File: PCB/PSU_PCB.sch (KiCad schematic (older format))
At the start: 116 parts, among them P1 Bluetooth HM-10, P2 ISP, P3 V+, P4 V-, Q1 IRLML0030TRPBF, Q2 IRLML0030TRPBF, SW1 SW_PUSH_SMALL_H, U1 OPA2170, U10 LT3080, U11 LM334M, U2 USB_TYPE_C, U3 ATMEGA32U4RC-A, U4 MCP41010, U5 LT1370, U6 MAX6610, U7 OPA4170, U8 INA219, U9 MCP1252, Y1 16Mhz

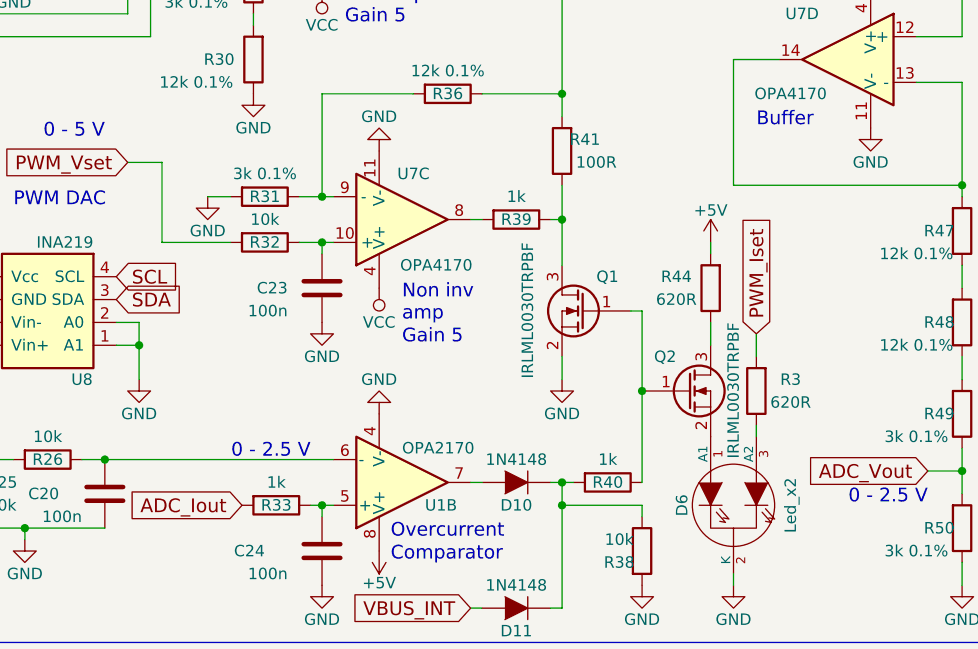
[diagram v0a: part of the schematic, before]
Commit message: Fixed minor PCB error Adjusted code for current measurement
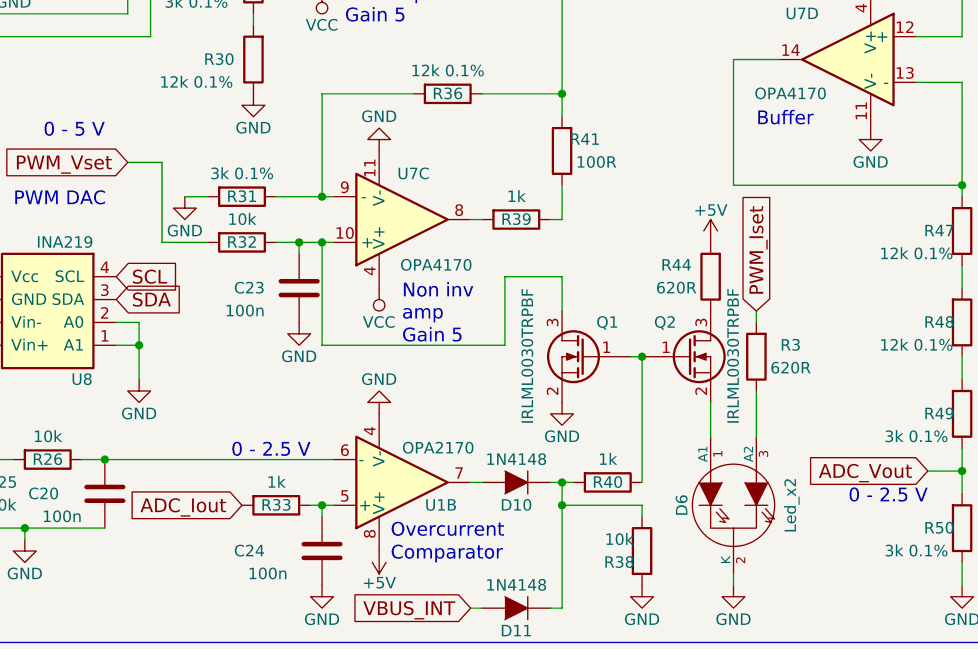
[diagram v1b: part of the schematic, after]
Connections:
- net at C23.2, R32.1, U7.10 (+): now also Q1.3 (D)
- net at R39.1, R41.1: no longer Q1.3 (D)
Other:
- moved on the sheet: C23, Q1, Q2, R3, R31, R32, R44
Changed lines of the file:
@@
 L R R31
 U 1 1 57B3FFF3
-P 7800 3200
-F 0 "R31" V 7800 3200 50  0000 C CNN
-F 1 "3k 0.1%" V 7700 3200 50  0000 C CNN
-F 2 "Resistors_SMD:R_0603_HandSoldering" V 7730 3200 50  0001 C CNN
-F 3 "" H 7800 3200 50  0000 C CNN
-	1    7800 3200
+P 7700 3200
+F 0 "R31" V 7700 3200 50  0000 C CNN
+F 1 "3k 0.1%" V 7600 3200 50  0000 C CNN
+F 2 "Resistors_SMD:R_0603_HandSoldering" V 7630 3200 50  0001 C CNN
+F 3 "" H 7700 3200 50  0000 C CNN
+	1    7700 3200
 	0    1    1    0
 $EndComp
@@
 L GND #PWR015
 U 1 1 57B40093
-P 7550 3200
-F 0 "#PWR015" H 7550 2950 50  0001 C CNN
-F 1 "GND" H 7550 3050 50  0000 C CNN
-F 2 "" H 7550 3200 50  0000 C CNN
-F 3 "" H 7550 3200 50  0000 C CNN
-	1    7550 3200
+P 7450 3200
+F 0 "#PWR015" H 7450 2950 50  0001 C CNN
+F 1 "GND" H 7450 3050 50  0000 C CNN
+F 2 "" H 7450 3200 50  0000 C CNN
+F 3 "" H 7450 3200 50  0000 C CNN
+	1    7450 3200
 	1    0    0    -1
 $EndComp
@@
 L R R32
 U 1 1 57B47B3D
-P 7800 3400
-F 0 "R32" V 7800 3400 50  0000 C CNN
-F 1 "10k" V 7700 3400 50  0000 C CNN
-F 2 "Resistors_SMD:R_0603_HandSoldering" V 7730 3400 50  0001 C CNN
-F 3 "" H 7800 3400 50  0000 C CNN
-	1    7800 3400
+P 7700 3400
+F 0 "R32" V 7700 3400 50  0000 C CNN
+F 1 "10k" V 7600 3400 50  0000 C CNN
+F 2 "Resistors_SMD:R_0603_HandSoldering" V 7630 3400 50  0001 C CNN
+F 3 "" H 7700 3400 50  0000 C CNN
+	1    7700 3400
 	0    1    1    0
 $EndComp
@@
 L C C23
 U 1 1 57B48497
-P 8050 3600
-F 0 "C23" H 8200 3600 50  0000 L CNN
-F 1 "100n" H 8200 3700 50  0000 L CNN
-F 2 "Capacitors_SMD:C_0603_HandSoldering" H 8088 3450 50  0001 C CNN
-F 3 "" H 8050 3600 50  0000 C CNN
-	1    8050 3600
+P 7950 3600
+F 0 "C23" H 8100 3600 50  0000 L CNN
+F 1 "100n" H 8100 3700 50  0000 L CNN
+F 2 "Capacitors_SMD:C_0603_HandSoldering" H 7988 3450 50  0001 C CNN
+F 3 "" H 7950 3600 50  0000 C CNN
+	1    7950 3600
 	-1   0    0    1
 $EndComp
@@
 L GND #PWR016
 U 1 1 57B48873
-P 8050 3750
-F 0 "#PWR016" H 8050 3500 50  0001 C CNN
-F 1 "GND" H 8050 3600 50  0000 C CNN
-F 2 "" H 8050 3750 50  0000 C CNN
-F 3 "" H 8050 3750 50  0000 C CNN
-	1    8050 3750
+P 7950 3750
+F 0 "#PWR016" H 7950 3500 50  0001 C CNN
+F 1 "GND" H 7950 3600 50  0000 C CNN
+F 2 "" H 7950 3750 50  0000 C CNN
+F 3 "" H 7950 3750 50  0000 C CNN
+	1    7950 3750
 	1    0    0    -1
 $EndComp
@@
 L R R44
 U 1 1 57B99CDC
-P 9750 3600
-F 0 "R44" H 9900 3550 50  0000 C CNN
-F 1 "620R" H 9900 3650 50  0000 C CNN
-F 2 "Resistors_SMD:R_0603_HandSoldering" V 9680 3600 50  0001 C CNN
-F 3 "" H 9750 3600 50  0000 C CNN
-	1    9750 3600
+P 9750 3550
+F 0 "R44" H 9900 3500 50  0000 C CNN
+F 1 "620R" H 9900 3600 50  0000 C CNN
+F 2 "Resistors_SMD:R_0603_HandSoldering" V 9680 3550 50  0001 C CNN
+F 3 "" H 9750 3550 50  0000 C CNN
+	1    9750 3550
 	-1   0    0    1
 $EndComp
@@
 8E D2 4E 06 E9 83 31 0C B8 01 D4 62 7A FA FE CA 1E E7 AB A8 50 4D B8 D1 52 86 A6 EF 44 4C F7 6B
 69 A6 CB 4C 71 E1 73 B8 2B 4F 00 E7 75 28 F9 2E A2 C6 63 AC 40 DB 07 B2 19 61 39 9A 3C 4A F1 B4
-F5 AD 2E B3 0D FC 7F 6D 80 3F 3C 28 70 B1 D5 00 00 00 00 49 45 4E 44 AE 42 60 82 D1
+F5 AD 2E B3 0D FC 7F 6D 80 3F 3C 28 70 B1 D5 00 00 00 00 49 45 4E 44 AE 42 60 82 66
 EndData
 $EndBitmap
@@
 00 09 E8 04 41 10 04 61 00 48 40 27 08 82 20 08 03 40 02 3A 41 10 04 41 18 00 23 00 F5 5D DD 09
 82 20 08 82 20 B4 52 CF 06 60 0D 60 1C 9A D7 A4 13 04 41 10 04 D1 BD 50 00 7E F8 7F 36 C9 A5 48
-A4 FE A8 58 00 00 00 00 49 45 4E 44 AE 42 60 82 20
+A4 FE A8 58 00 00 00 00 49 45 4E 44 AE 42 60 82 40
 EndData
 $EndBitmap
@@
 L GND #PWR038
 U 1 1 58E93020
-P 9100 4000
-F 0 "#PWR038" H 9100 3750 50  0001 C CNN
-F 1 "GND" H 9100 3850 50  0000 C CNN
-F 2 "" H 9100 4000 50  0000 C CNN
-F 3 "" H 9100 4000 50  0000 C CNN
-	1    9100 4000
+P 9100 4100
+F 0 "#PWR038" H 9100 3850 50  0001 C CNN
+F 1 "GND" H 9100 3950 50  0000 C CNN
+F 2 "" H 9100 4100 50  0000 C CNN
+F 3 "" H 9100 4100 50  0000 C CNN
+	1    9100 4100
 	1    0    0    -1
 $EndComp
@@
 L Q_NMOS_GSD Q1
 U 1 1 59B69DD1
-P 9200 3700
-F 0 "Q1" H 9150 3850 50  0000 R CNN
-F 1 "IRLML0030TRPBF" V 9450 4000 50  0000 R CNN
-F 2 "TO_SOT_Packages_SMD:SOT-23" H 9400 3800 50  0001 C CNN
-F 3 "" H 9200 3700 50  0000 C CNN
-	1    9200 3700
+P 9200 3900
+F 0 "Q1" H 9150 4050 50  0000 R CNN
+F 1 "IRLML0030TRPBF" V 9450 4200 50  0000 R CNN
+F 2 "TO_SOT_Packages_SMD:SOT-23" H 9400 4000 50  0001 C CNN
+F 3 "" H 9200 3900 50  0000 C CNN
+	1    9200 3900
 	-1   0    0    -1
 $EndComp
@@
 L Q_NMOS_GSD Q2
 U 1 1 59C405FE
-P 9650 4050
-F 0 "Q2" H 9600 4200 50  0000 R CNN
-F 1 "IRLML0030TRPBF" V 9850 4350 50  0000 R CNN
-F 2 "TO_SOT_Packages_SMD:SOT-23" H 9850 4150 50  0001 C CNN
-F 3 "" H 9650 4050 50  0000 C CNN
-	1    9650 4050
+P 9650 3900
+F 0 "Q2" H 9600 4050 50  0000 R CNN
+F 1 "IRLML0030TRPBF" V 9850 4200 50  0000 R CNN
+F 2 "TO_SOT_Packages_SMD:SOT-23" H 9850 4000 50  0001 C CNN
+F 3 "" H 9650 3900 50  0000 C CNN
+	1    9650 3900
 	1    0    0    -1
 $EndComp
@@
 	0    -1   -1   0
 $EndComp
-Text GLabel 9950 3800 1    60   Input ~ 0
+Text GLabel 9950 3700 1    60   Input ~ 0
 PWM_Iset
 $Comp
 L R R3
 U 1 1 59D48892
-P 9950 4050
-F 0 "R3" H 9800 4000 50  0000 C CNN
-F 1 "620R" H 9800 4100 50  0000 C CNN
-F 2 "Resistors_SMD:R_0603_HandSoldering" V 9880 4050 50  0001 C CNN
-F 3 "" H 9950 4050 50  0000 C CNN
-	1    9950 4050
+P 9950 3900
+F 0 "R3" H 9800 3850 50  0000 C CNN
+F 1 "620R" H 9800 3950 50  0000 C CNN
+F 2 "Resistors_SMD:R_0603_HandSoldering" V 9880 3900 50  0001 C CNN
+F 3 "" H 9950 3900 50  0000 C CNN
+	1    9950 3900
 	-1   0    0    1
 $EndComp
@@
 Wire Wire Line
 	9850 4900 9850 4850
-Connection ~ 9450 4050
+Connection ~ 9450 3900
 Wire Wire Line
 	8750 4450 8700 4450
@@
 	5350 3650 4100 3650
 Wire Wire Line
-	9950 3900 9950 3800
+	9950 3750 9950 3700
 Wire Wire Line
-	9950 4250 9950 4200
+	9950 4250 9950 4050
 Wire Wire Line
 	4300 2650 4300 2150
@@
 	9850 3150 9850 2600
 Wire Wire Line
-	7350 3400 7650 3400
+	7350 3400 7550 3400
 Wire Wire Line
 	6500 3650 6500 4000
@@
 Connection ~ 10600 1050
 Wire Wire Line
-	9750 3750 9750 3850
+	9750 3700 9750 3700
 Connection ~ 6200 1050
 Wire Wire Line
@@
 Connection ~ 10000 1050
 Wire Wire Line
-	7550 3200 7650 3200
+	7450 3200 7550 3200
 Wire Wire Line
-	7950 3200 8100 3200
-Wire Wire Line
-	9100 3150 9100 3500
+	7850 3200 8100 3200
 Connection ~ 8050 3200
 Wire Wire Line
@@
 Connection ~ 9100 2750
 Wire Wire Line
-	7950 3400 8100 3400
+	7850 3400 8100 3400
 Wire Wire Line
-	8050 3450 8050 3400
-Connection ~ 8050 3400
-Connection ~ 9100 3300
+	7950 3450 7950 3400
+Connection ~ 7950 3400
 Wire Wire Line
 	8000 4550 8100 4550
@@
 	6350 3550 6550 3550
 Wire Wire Line
-	9750 3400 9750 3450
+	9750 3400 9750 3400
 Wire Wire Line
 	4200 3000 4950 3000
@@
 Connection ~ 10150 1850
 Wire Wire Line
-	9100 3900 9100 4000
-Wire Wire Line
 	4200 2900 5150 2900
 Wire Wire Line
@@
 	6950 7750 6950 6750
 Wire Wire Line
-	9450 3700 9400 3700
+	9450 3900 9400 3900
 Wire Wire Line
 	9050 4450 9150 4450
@@
 	9100 5000 9050 5000
 Wire Wire Line
-	9450 3700 9450 4450
+	9450 3900 9450 4450
 Wire Wire Line
 	9450 4600 9450 4550
@@
 Wire Wire Line
 	1200 4200 1200 4250
+Wire Wire Line
+	9100 3300 9100 3150
+Wire Wire Line
+	9750 4250 9750 4100
+Wire Wire Line
+	8050 3400 8050 3850
+Connection ~ 8050 3400
+Wire Wire Line
+	8050 3850 8850 3850
+Wire Wire Line
+	8850 3850 8850 3550
+Wire Wire Line
+	8850 3550 9100 3550
+Wire Wire Line
+	9100 3550 9100 3700
 $EndSCHEMATC
